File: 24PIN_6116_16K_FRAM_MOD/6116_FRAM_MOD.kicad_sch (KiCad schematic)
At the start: 18 parts, among them J1 Conn_01x02, U1 TL431DBZ, U10 TC5564APL_Adapter, U2 74AHC2G00, U3 STK12C68

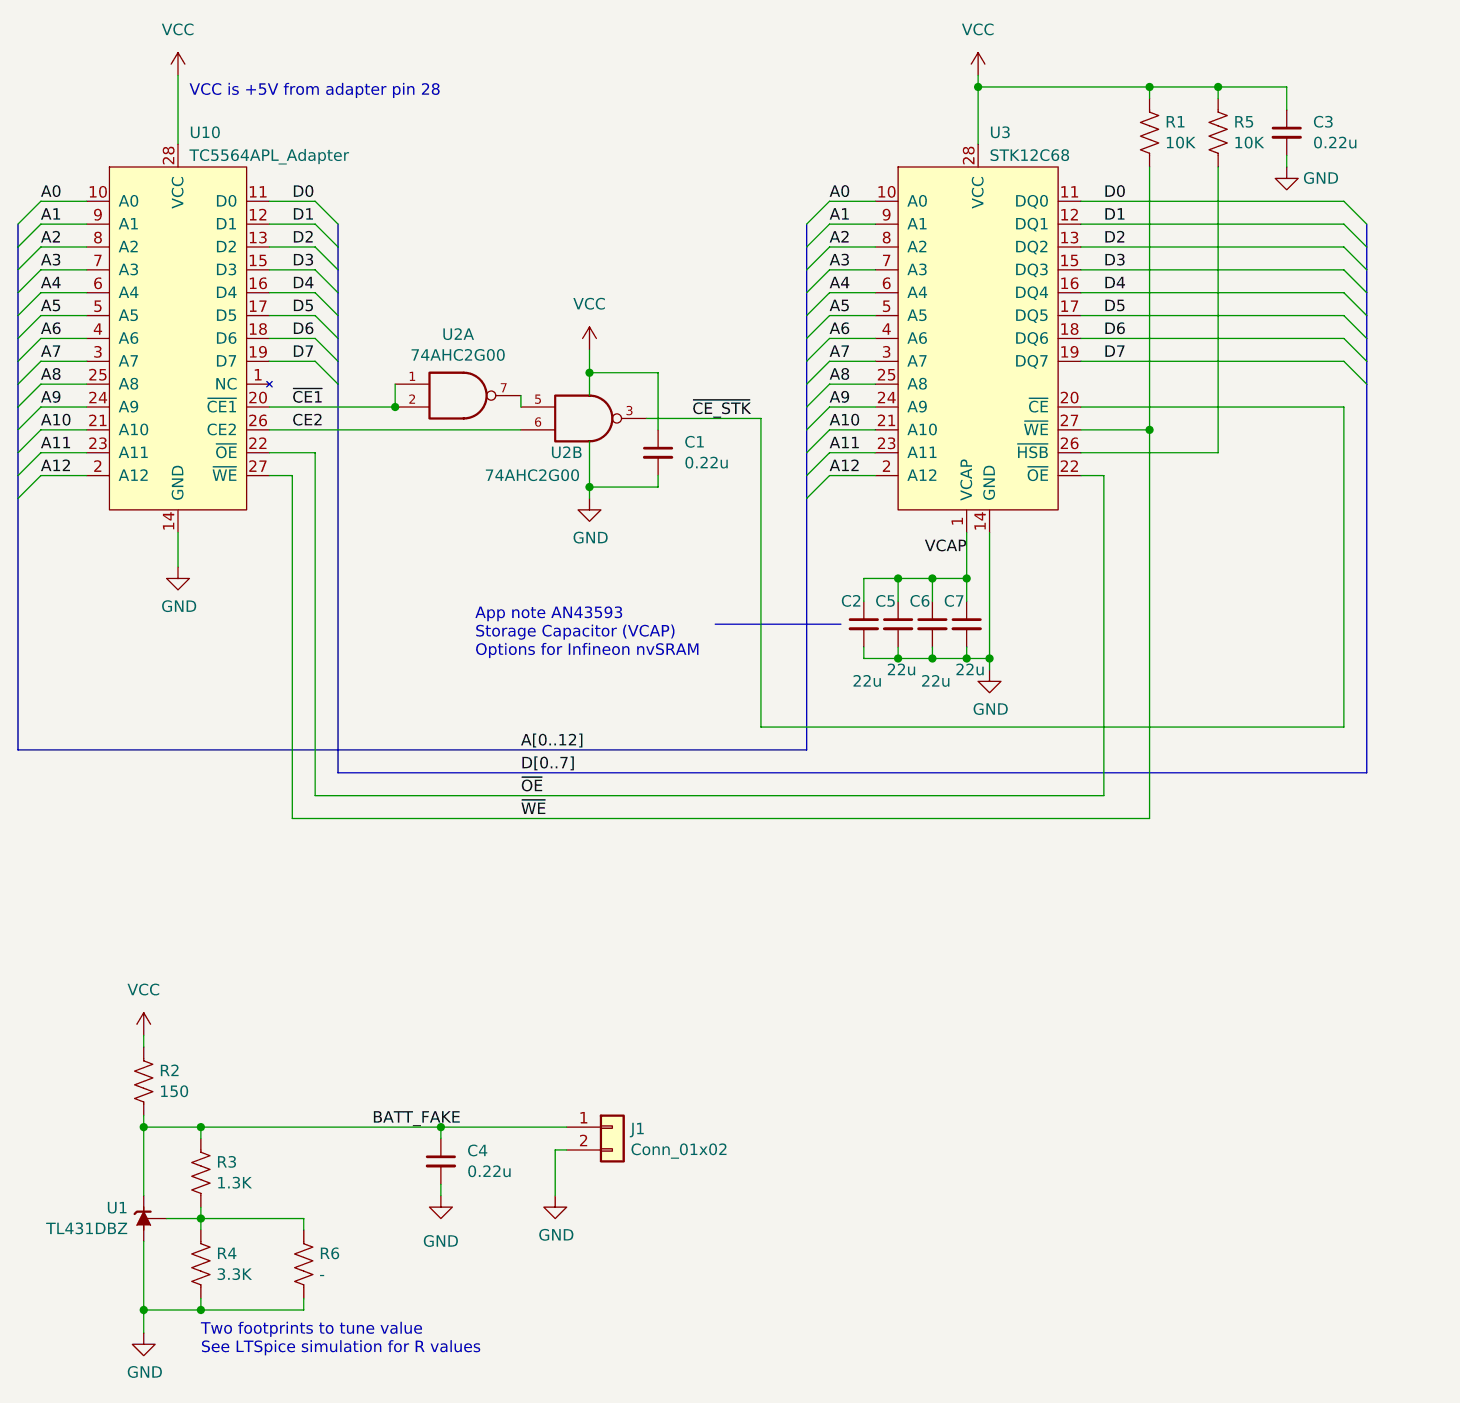
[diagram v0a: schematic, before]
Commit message: Finished 24PIN 6116 version.
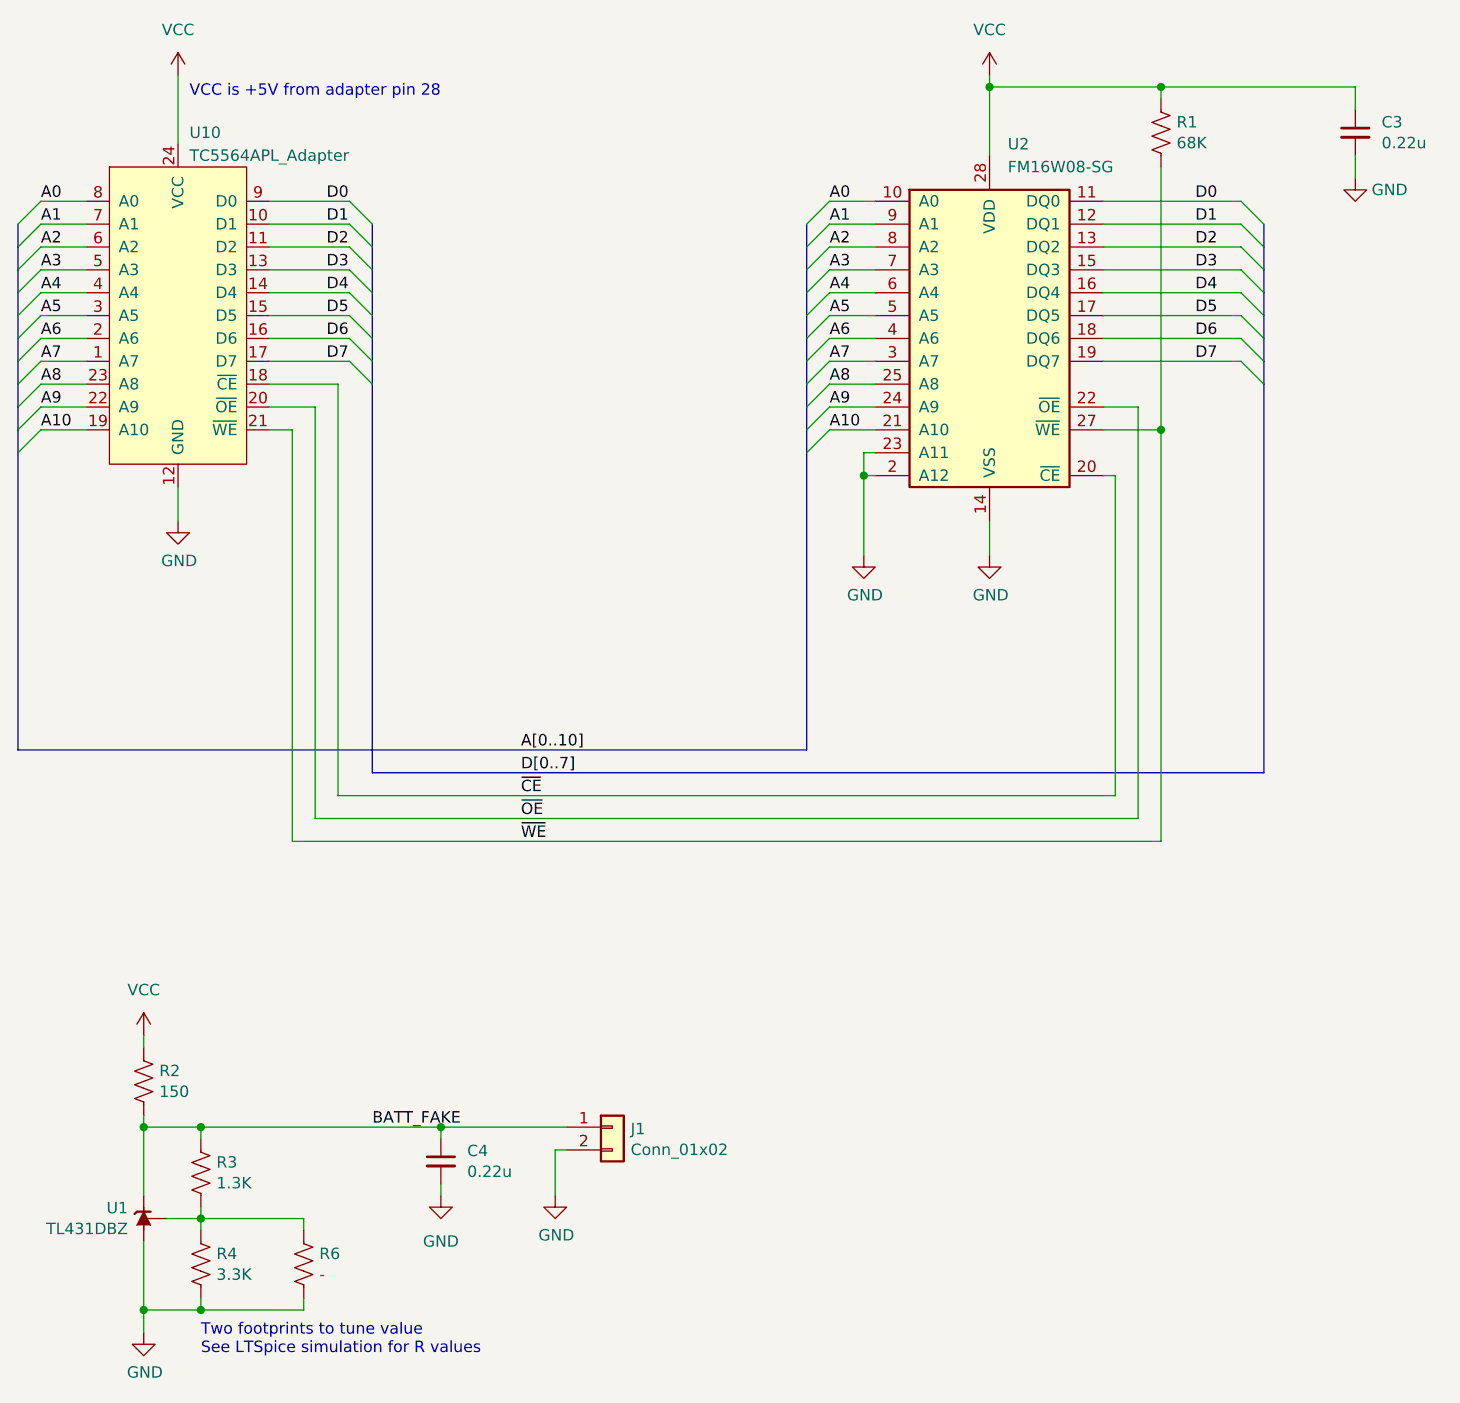
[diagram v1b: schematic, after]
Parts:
- removed C1: 0.22u, Capacitor_SMD:C_0603_1608Metric, symbol Device:C_Small
- removed C2, C5, C6, C7: 22u, Capacitor_SMD:C_0603_1608Metric, symbol Device:C_Small
- removed R5: 10K, Resistor_SMD:R_0402_1005Metric_Pad0.72x0.64mm_HandSolder, symbol Device:R_US
- removed U2: 74AHC2G00, Package_SO:TSSOP-8_3x3mm_P0.65mm, symbol 74xGxx:74AHC2G00
- removed U3: STK12C68, Package_SO_Cypress:SOIC-28W_8.7x18.4mm_P1.27mm, symbol Memory_NVRAM_Cypress:STK12C68
- added U2: FM16W08-SG, Package_SO:SOIC-28W_7.5x17.9mm_P1.27mm, symbol Memory_NVRAM:FM16W08-SG
- R1: value 10K -> 68K
- U10: footprint Package_DIP_Adapter:DIP-28_W15.24mm_Socket_Adapter -> Package_DIP_Adapter:DIP-24_W15.24mm_Socket_Adapter; symbol Memory_RAM_Toshiba:TC5564APL_Adapter -> Memory_RAM_Toshiba:TC5517APL_Adapter
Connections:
- net A11 is gone; now on net A8: U10.23 (A8)
- net A12 is gone; now on net A6: U10.2 (A6)
- net ~{CE1} is gone; now on net ~{OE}: U10.20 (~{OE})
- net A0: now also U10.8 (A0), U2.10 (A0); no longer U10.10 (A0)
- net A1: now also U10.7 (A1), U2.9 (A1); no longer U10.9 (A1)
- net A10: now also U10.19 (A10), U2.21 (A10); no longer U10.21 (A10)
- net A2: now also U10.6 (A2), U2.8 (A2); no longer U10.8 (A2)
- net A3: now also U10.5 (A3), U2.7 (A3); no longer U10.7 (A3)
- net A4: now also U10.4 (A4), U2.6 (A4); no longer U10.6 (A4)
- net A5: now also U10.3 (A5), U2.5 (A5); no longer U10.5 (A5)
- net A6: now also U2.4 (A6); no longer U10.4 (A6)
- net A7: now also U10.1 (A7), U2.3 (A7); no longer U10.3 (A7)
- net A8: now also U2.25 (A8); no longer U10.25 (A8)
- net A9: now also U10.22 (A9), U2.24 (A9); no longer U10.24 (A9)
- net D0: now also U10.9 (D0), U2.11 (DQ0); no longer U10.11 (D0)
- net D1: now also U10.10 (D1), U2.12 (DQ1); no longer U10.12 (D1)
- net D2: now also U10.11 (D2), U2.13 (DQ2); no longer U10.13 (D2)
- net D3: now also U10.13 (D3), U2.15 (DQ3); no longer U10.15 (D3)
- net D4: now also U10.14 (D4), U2.16 (DQ4); no longer U10.16 (D4)
- net D5: now also U10.15 (D5), U2.17 (DQ5); no longer U10.17 (D5)
- net D6: now also U10.16 (D6), U2.18 (DQ6); no longer U10.18 (D6)
- net D7: now also U10.17 (D7), U2.19 (DQ7); no longer U10.19 (D7)
- net GND: now also U10.12 (GND), U2.14 (VSS), U2.2 (A12), U2.23 (A11); no longer U10.14 (GND)
- net VCC: now also U10.24 (VCC), U2.28 (VDD); no longer U10.28 (VCC)
- net ~{OE}: now also U2.22 (~{OE}); no longer U10.22 (~{OE})
- net ~{WE}: now also U10.21 (~{WE}), U2.27 (~{WE}); no longer U10.27 (~{WE})
- removed net CE2: U10.26 (CE2)
- new net ~{CE}: U10.18 (~{CE}), U2.20 (~{CE})
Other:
- note removed: "App note AN43593 Storage Capacitor (VCAP) Options for Infineon nvSRAM"
- moved on the sheet: C3, R1

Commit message: Updated title block on schematics. Minor silkscreen tweak to 24PIN 6116
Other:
- title: (none) -> 6116_NVSRAM_MOD
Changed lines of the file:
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@@
 (kicad_sch (version 20211123) (generator eeschema)
   (paper "USLetter")
+  (title_block
+    (title "6116_NVSRAM_MOD")
+    (date "2022-11-12")
+    (rev "V1.0.1")
+    (comment 1 "Copyright Dr. Matthew Swabey")
+    (comment 2 "Touched up silkscreen")
+  )
   (junction (at 68.58 175.26) (diameter 0) (color 0 0 0 0)
   )
